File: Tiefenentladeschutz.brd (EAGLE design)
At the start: 60 x 60 mm, 25 parts, among them IC1 ICL7665CSA, Q4 NMOSFET-D2PAK-7

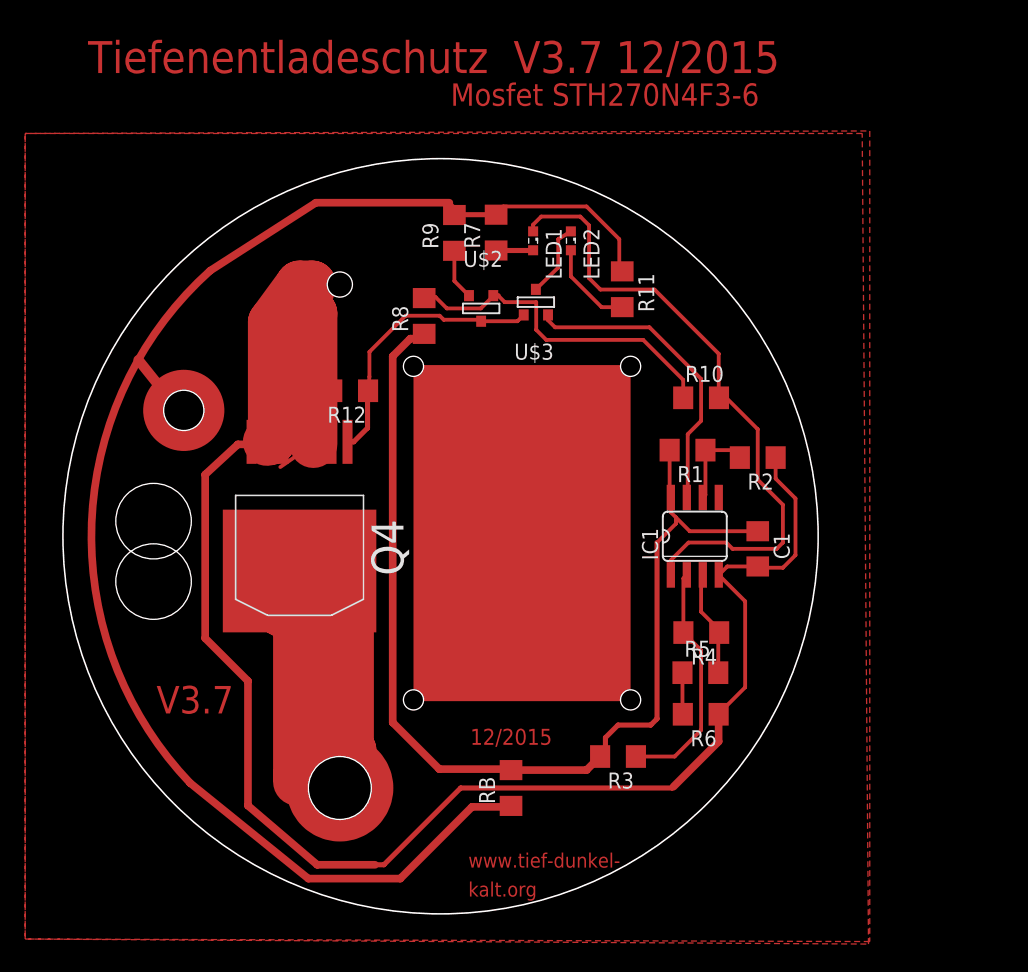
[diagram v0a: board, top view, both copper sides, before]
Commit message: Added Mosfet Gate Resistors
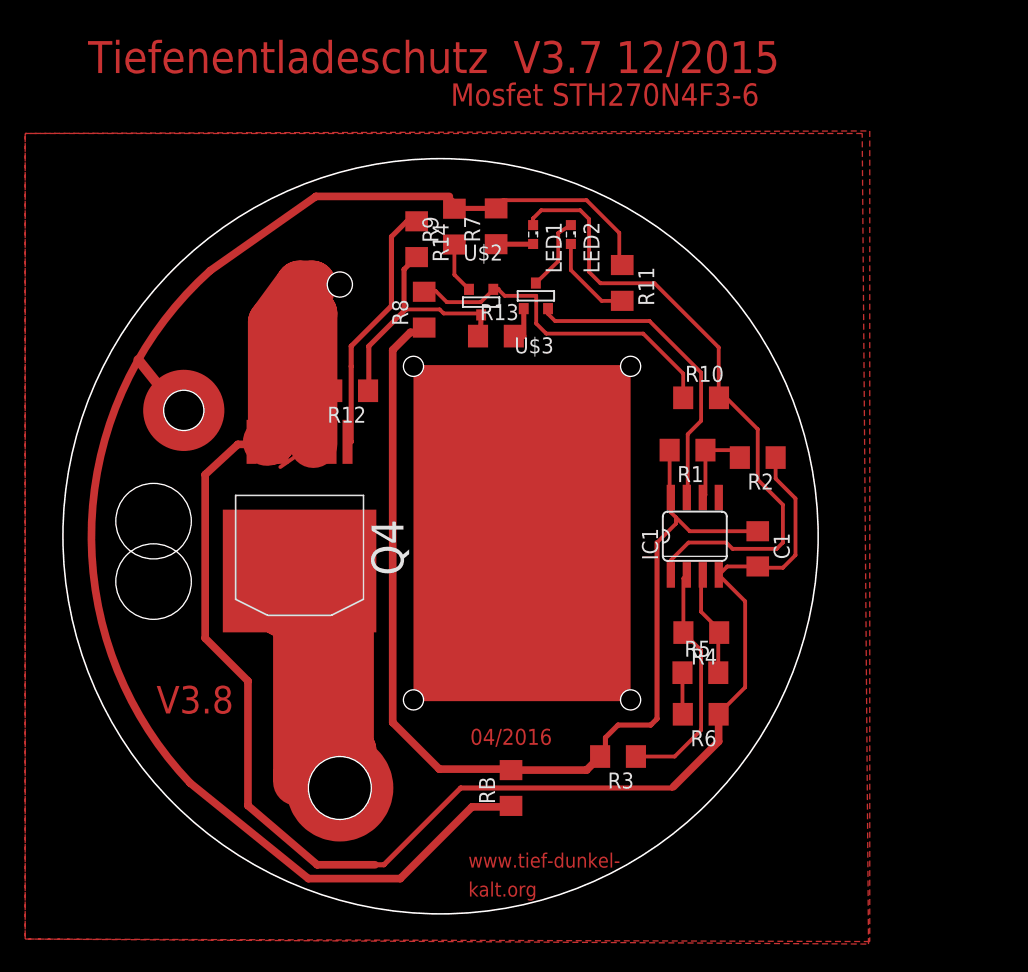
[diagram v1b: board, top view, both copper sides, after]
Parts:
- added R13, R14: 100, eagle-ltspice:R1206
- moved LED1 0.50 mm to (37.4, 54.0)
- moved LED2 0.50 mm to (40.4, 54.0)
- moved R11 0.50 mm to (44.4, 50.1)
- moved R7 0.50 mm to (34.4, 54.6)
- moved R8 0.50 mm to (28.7, 48.0)
- moved R9 0.50 mm to (31.1, 54.6)
- moved U$2 0.50 mm to (33.2, 48.6)
- moved U$3 0.50 mm to (37.6, 49.1)
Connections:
- new net N$12: Q4.G, R14.1
- new net N$9: R13.2, U$3.3
- net N$22: now also R13.1, R14.2; no longer Q4.G, U$3.3
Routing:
- net N$12: track 0.00 -> 20.4 mm
- net N$9: track 0.00 -> 2.99 mm
- net N$22: track 22.0 -> 21.4 mm
- net V+: track 115.7 -> 116.2 mm
- net N$7: track 26.9 -> 27.4 mm
- net N$3: track 24.4 -> 24.9 mm
- net N$16: track 51.0 -> 51.5 mm
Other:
- board text added: "04/2016"
- board text added: "V3.8"
- board text removed: "12/2015"
- board text removed: "V3.7"

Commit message: Ohne LED added, replaced P-mosfet by bipolar
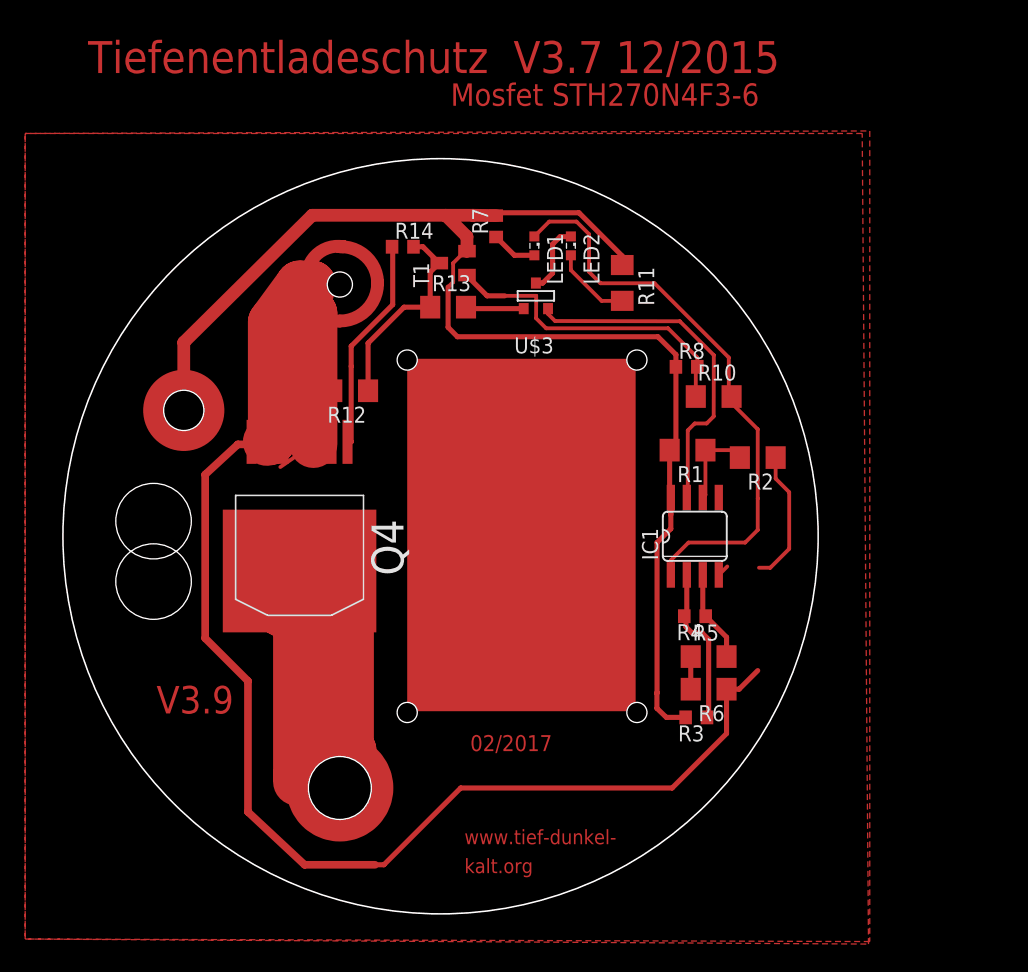
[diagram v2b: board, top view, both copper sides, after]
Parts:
- removed C1: 100 nF, eagle-ltspice:C1206
- removed R9: 68k, eagle-ltspice:R1206
- removed RB: 0, eagle-ltspice:R1206
- removed U$2: IRLML9301, 0liver:SOT-23
- added T1: BC856B, transistor:SOT23-BEC
- R10: value 68k -> 12k
- R12: value 100k -> 20k
- R13: device eagle-ltspice:R1206 -> rcl:R1206
- R14: value 100 -> 10; device eagle-ltspice:R1206 -> rcl:R0603
- R3, R4, R7: device eagle-ltspice:R1206 -> rcl:R0603
- R8: value 470k -> 20k; device eagle-ltspice:R1206 -> rcl:R0603
- moved R8 21.3 mm to (49.5, 43.5), turned to 0 degrees
- moved R3 6.95 mm to (50.3, 15.6)
- moved R13 4.44 mm to (30.6, 48.2)
- moved R6 2.09 mm to (51.3, 17.9)
- moved R5 1.44 mm to (51.3, 20.4)
- moved R4 1.39 mm to (50.2, 23.6)
- moved R14 1.25 mm to (27.0, 53.0), turned to 0 degrees
- moved R10 1.00 mm to (51.7, 41.1)
- moved LED1 0.91 mm to (37.5, 53.1)
- moved LED2 0.90 mm to (40.4, 53.1)
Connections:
- removed net N$10: R9.2, RB.1
- removed net N$8: R9.1, U$2.2
- net GND: no longer C1.2
- net N$22: now also T1.C; no longer U$2.1
- net N$7: now also T1.B; no longer U$2.3
- net V+: now also T1.E; no longer C1.1, RB.2
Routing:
- net N$10: track 94.7 -> 0.00 mm
- net GND: track 153.9 -> 168.0 mm
- net N$13: track 19.1 -> 12.7 mm
- net N$16: track 51.5 -> 46.8 mm
- net N$22: track 21.4 -> 16.9 mm
- net N$8: track 4.04 -> 0.00 mm
- net N$12: track 20.4 -> 16.8 mm
- net N$3: track 24.9 -> 27.7 mm
- net N$7: track 27.4 -> 25.7 mm
- net N$9: track 2.99 -> 4.64 mm
- net N$2: track 8.45 -> 7.27 mm
- net N$5: track 7.17 -> 6.27 mm
- net N$26: track 3.32 -> 2.59 mm
- net N$6: track 2.95 -> 3.64 mm
- net V+: track 116.2 -> 115.6 mm
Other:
- board text added: "02/2017"
- board text added: "V3.9"
- board text removed: "04/2016"
- board text removed: "V3.8"

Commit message: R12 to 100 kOhm
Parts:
- R12: value 20k -> 100k
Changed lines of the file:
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@@
 <element name="U$5" library="0liver" package="LEER" value="PIN-GENERIC" x="0.5" y="0.5"/>
 <element name="R3" library="rcl" package="R0603" value="100k" x="50.32" y="15.61" rot="R180"/>
-<element name="R12" library="eagle-ltspice" package="R1206" value="20k" x="22.82" y="41.56" rot="R180">
+<element name="R12" library="eagle-ltspice" package="R1206" value="100k" x="22.82" y="41.56" rot="R180">
 <attribute name="SPICEMODEL" value="NONE" x="22.82" y="41.56" size="1.778" layer="27" rot="R180" display="off"/>
 <attribute name="SPICEPREFIX" value="R" x="22.82" y="41.56" size="1.778" layer="27" rot="R180" display="off"/>

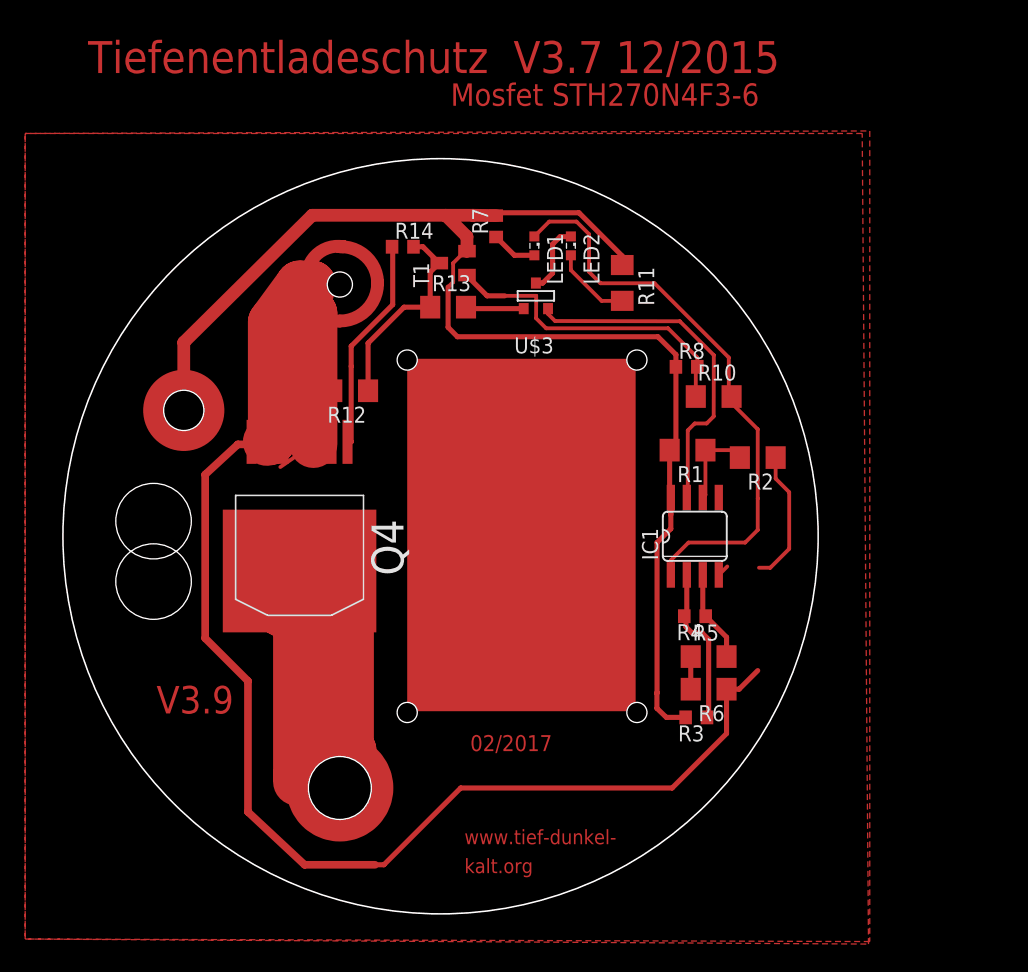
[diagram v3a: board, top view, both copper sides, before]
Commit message: Smaller Resistors, less transistors, smaller pcb
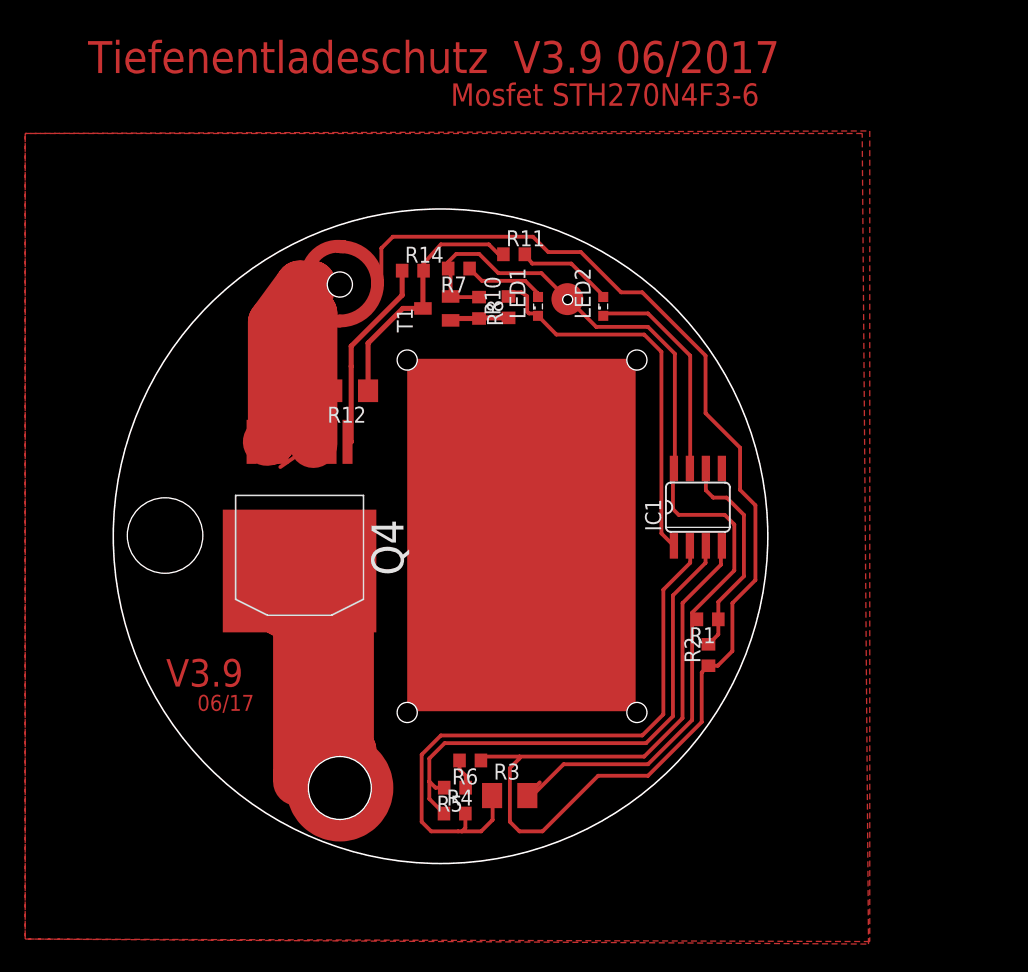
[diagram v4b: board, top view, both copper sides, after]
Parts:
- removed R13: 100, rcl:R1206
- removed U$3: IRLML6346, 0liver:SOT-23
- R1, R10, R11, R2, R5, R6: device eagle-ltspice:R1206 -> rcl:R0603
- R3: device rcl:R0603 -> rcl:M1206
- moved U$4 31.7 mm to (40.1, 48.8)
- moved R4 24.7 mm to (31.1, 7.97), turned to 0 degrees
- moved R5 22.7 mm to (31.1, 10.0), turned to 180 degrees
- moved R6 19.8 mm to (32.4, 12.2)
- moved R10 17.8 mm to (35.4, 48.2), turned to 90 degrees
- moved R8 17.1 mm to (33.1, 48.1), turned to 270 degrees
- moved R2 16.2 mm to (51.3, 20.6), turned to 90 degrees
- moved R3 16.1 mm to (35.5, 9.40), turned to 0 degrees
- moved R1 13.5 mm to (51.2, 23.4)
- moved R11 8.89 mm to (35.8, 52.4), turned to 0 degrees
- moved LED2 5.46 mm to (42.9, 48.3), turned to 90 degrees
- moved LED1 4.82 mm to (37.7, 48.3), turned to 90 degrees
- moved R7 4.47 mm to (31.5, 51.3), turned to 180 degrees
- moved T1 3.83 mm to (29.7, 48.1)
- moved IC1 2.32 mm to (50.4, 32.3)
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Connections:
- removed net N$11: LED2.C, U$3.1
- removed net N$9: R13.2, U$3.3
- net N$22: now also R11.1; no longer R13.1
- net N$3: now also LED2.C; no longer U$3.2
- net V+: no longer R11.1
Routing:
- net N$13: track 12.7 -> 50.0 mm
- net V+: track 115.6 -> 78.9 mm
- net N$2: track 7.27 -> 41.6 mm
- net GND: track 168.0 -> 194.6 mm
- net N$7: track 25.7 -> 4.68 mm
- net N$16: track 46.8 -> 30.8 mm
- net N$3: track 27.7 -> 17.4 mm
- net N$4: track 6.83 -> 17.0 mm
- net N$11: track 5.66 -> 0.00 mm
- net N$9: track 4.64 -> 0.00 mm
- net N$22: track 16.9 -> 20.9 mm
- net N$6: track 3.64 -> 6.51 mm
- net N$5: track 6.27 -> 7.75 mm
- net N$12: track 16.8 -> 15.6 mm
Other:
- board size 60 x 60 mm -> 52 x 52 mm
- board text added: "06/17"
- board text added: "Tiefenentladeschutz V3.9 06/2017"
- board text removed: "02/2017"
- board text removed: "Tiefenentladeschutz V3.7 12/2015"
- board text removed: "www.tief-dunkel- kalt.org"

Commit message: Some wiring adjustments
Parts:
- R1, R2: device rcl:R0603 -> resistor:R0603
- moved R3 0.93 mm to (35.6, 8.48)
- moved R5 0.93 mm to (31.0, 9.11)
- moved R6 0.93 mm to (32.2, 11.3)
- moved R4 0.93 mm to (31.0, 7.06)
- moved R2 0.68 mm to (51.0, 20.0)
- moved IC1 0.65 mm to (50.9, 32.8)
- moved R1 0.48 mm to (51.4, 22.9)
- moved U$4 0.30 mm to (40.4, 48.8)
- moved LED1 0.22 mm to (37.9, 48.4)
- moved LED2 0.22 mm to (42.8, 48.4)
- moved U$7 0.22 mm to (21.7, 14.2)
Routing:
- net N$13: track 50.0 -> 51.7 mm
- net N$4: track 17.0 -> 18.3 mm
- net N$2: track 41.6 -> 42.9 mm
- net V+: track 78.9 -> 80.0 mm
- net N$3: track 17.4 -> 18.1 mm
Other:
- board text added: "www.tief- dunkel-kalt.org"

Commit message: Breitere Leiterbahnen und Gehäuse Modell
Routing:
- net GND: track 195.0 -> 195.9 mm
